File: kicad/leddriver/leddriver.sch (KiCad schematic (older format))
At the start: 19 parts, among them J1 Conn_01x01_Male, J2 Conn_01x02_Male, Q1 2N3904, SW1 SW_Push, U1 TLC555xP, U2 TLC555xP

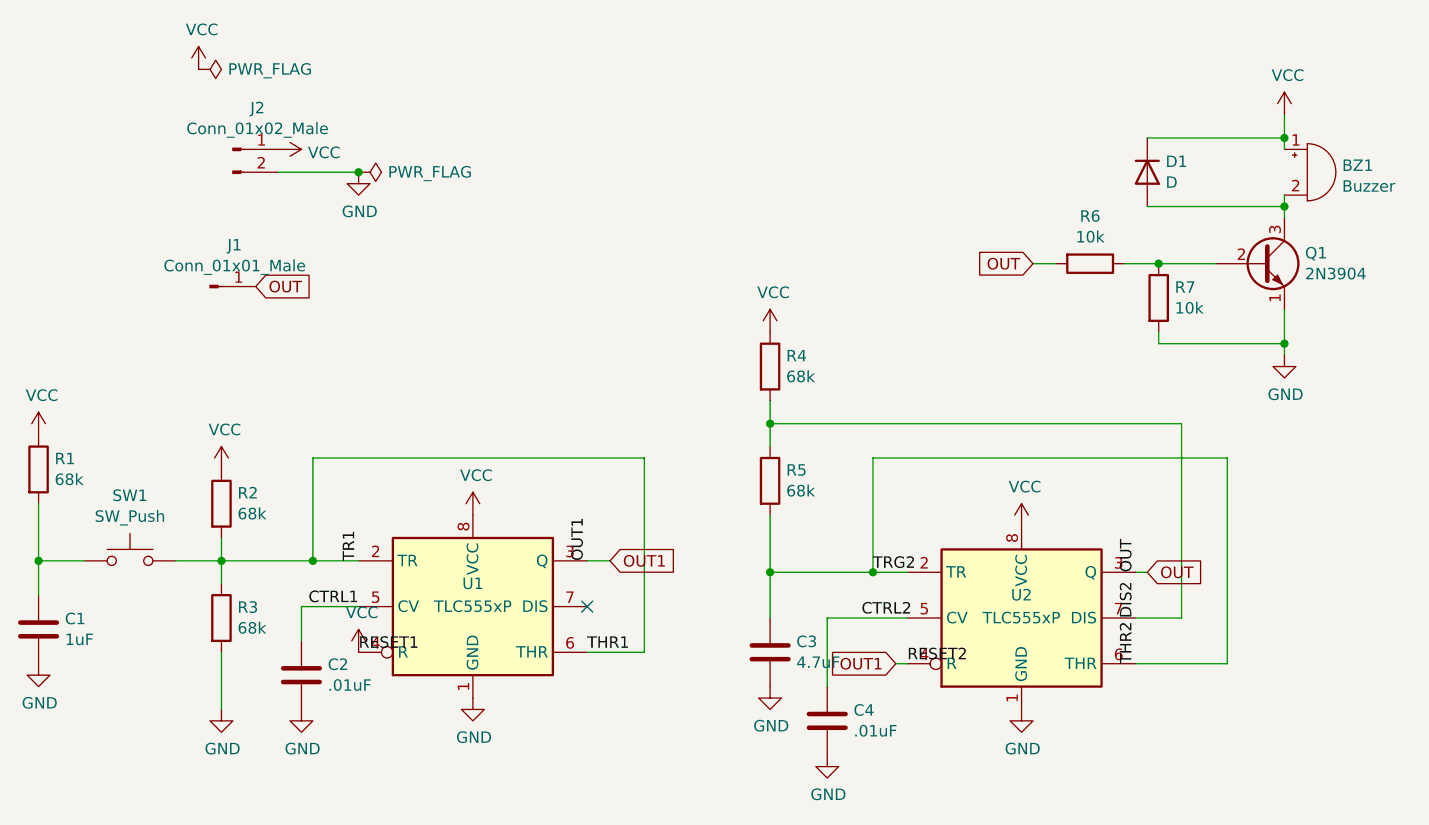
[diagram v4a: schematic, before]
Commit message: update according to new findings on breadboard.
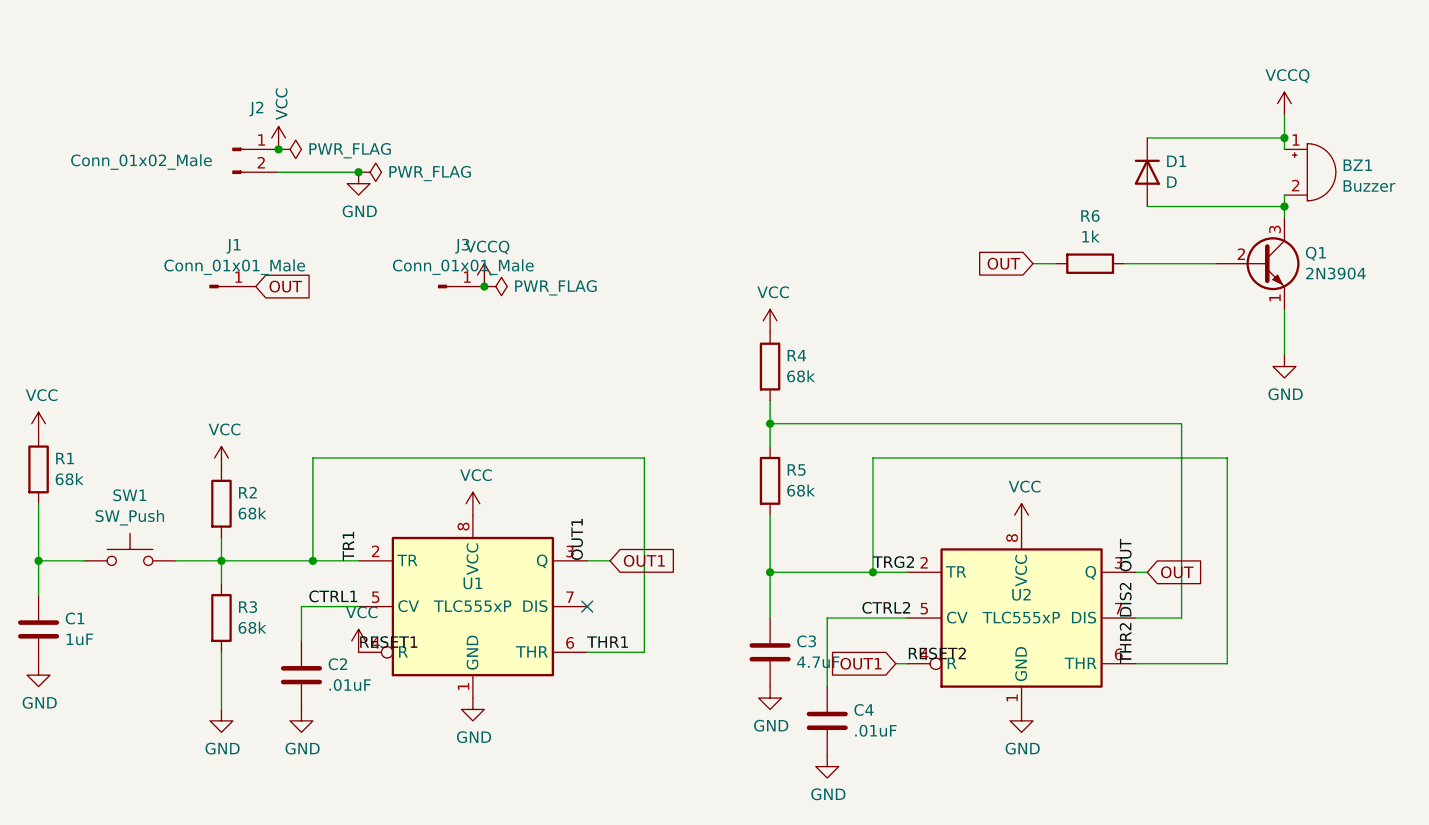
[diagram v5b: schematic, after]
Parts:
- removed R7: 10k, Resistor_THT:R_Axial_DIN0204_L3.6mm_D1.6mm_P2.54mm_Vertical, symbol Device:R
- added J3: Conn_01x01_Male, Connector_PinHeader_2.54mm:PinHeader_1x01_P2.54mm_Vertical, symbol Connector:Conn_01x01_Male
- R6: value 10k -> 1k
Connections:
- net VCC: no longer BZ1.1 (-), D1.1 (K)
- new net VCCQ: BZ1.1 (-), D1.1 (K), J3.1 (Pin_1)
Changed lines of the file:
@@
 L power:PWR_FLAG #FLG0101
 U 1 1 5F9073BF
-P 4350 750
-F 0 "#FLG0101" H 4350 825 50  0001 C CNN
-F 1 "PWR_FLAG" V 4350 878 50  0000 L CNN
-F 2 "" H 4350 750 50  0001 C CNN
-F 3 "~" H 4350 750 50  0001 C CNN
-	1    4350 750
+P 4700 1100
+F 0 "#FLG0101" H 4700 1175 50  0001 C CNN
+F 1 "PWR_FLAG" V 4700 1228 50  0000 L CNN
+F 2 "" H 4700 1100 50  0001 C CNN
+F 3 "~" H 4700 1100 50  0001 C CNN
+	1    4700 1100
 	0    1    1    0
 $EndComp
@@
 Text GLabel 8500 2950 2    50   Input ~ 0
 OUT
-$Comp
-L Connector:Conn_01x02_Male J2
-U 1 1 5F9522AD
-P 4500 1100
-F 0 "J2" H 4608 1281 50  0000 C CNN
-F 1 "Conn_01x02_Male" H 4608 1190 50  0000 C CNN
-F 2 "Connector_PinSocket_2.54mm:PinSocket_1x02_P2.54mm_Vertical" H 4500 1100 50  0001 C CNN
-F 3 "~" H 4500 1100 50  0001 C CNN
-	1    4500 1100
-	1    0    0    -1
-$EndComp
 Connection ~ 5050 1200
-$Comp
-L Connector:Conn_01x01_Male J1
-U 1 1 5F9568D2
-P 4400 1700
-F 0 "J1" H 4508 1881 50  0000 C CNN
-F 1 "Conn_01x01_Male" H 4508 1790 50  0000 C CNN
-F 2 "Connector_PinHeader_2.54mm:PinHeader_1x01_P2.54mm_Vertical" H 4400 1700 50  0001 C CNN
-F 3 "~" H 4400 1700 50  0001 C CNN
-	1    4400 1700
-	1    0    0    -1
-$EndComp
-$Comp
-L power:VCC #PWR0104
-U 1 1 5F974E8A
-P 4350 750
-F 0 "#PWR0104" H 4350 600 50  0001 C CNN
-F 1 "VCC" H 4365 923 50  0000 C CNN
-F 2 "" H 4350 750 50  0001 C CNN
-F 3 "" H 4350 750 50  0001 C CNN
-	1    4350 750
-	1    0    0    -1
-$EndComp
 $Comp
 L power:VCC #PWR0105
@@
 F 3 "" H 4700 1100 50  0001 C CNN
 	1    4700 1100
-	0    1    1    0
+	1    0    0    -1
 $EndComp
 $Comp
@@
 F 3 "" H 9100 2000 50  0001 C CNN
 	1    9100 2000
-	1    0    0    -1
-$EndComp
-$Comp
-L power:VCC #PWR0114
-U 1 1 5F9A00D1
-P 9100 950
-F 0 "#PWR0114" H 9100 800 50  0001 C CNN
-F 1 "VCC" H 9115 1123 50  0000 C CNN
-F 2 "" H 9100 950 50  0001 C CNN
-F 3 "" H 9100 950 50  0001 C CNN
-	1    9100 950
 	1    0    0    -1
 $EndComp
@@
 	9100 1050 9100 1100
 Wire Wire Line
-	9100 1800 9100 1950
-Wire Wire Line
 	4450 2900 4850 2900
 $Comp
@@
 	3650 2900 3650 3050
 $Comp
-L Device:R R7
-U 1 1 5F947F9D
-P 8550 1750
-F 0 "R7" H 8620 1796 50  0000 L CNN
-F 1 "10k" H 8620 1705 50  0000 L CNN
-F 2 "Resistor_THT:R_Axial_DIN0204_L3.6mm_D1.6mm_P2.54mm_Vertical" V 8480 1750 50  0001 C CNN
-F 3 "~" H 8550 1750 50  0001 C CNN
-	1    8550 1750
-	1    0    0    -1
-$EndComp
-$Comp
 L Device:R R6
 U 1 1 5F949B69
 P 8250 1600
 F 0 "R6" V 8043 1600 50  0000 C CNN
-F 1 "10k" V 8134 1600 50  0000 C CNN
+F 1 "1k" V 8134 1600 50  0000 C CNN
 F 2 "Resistor_THT:R_Axial_DIN0204_L3.6mm_D1.6mm_P2.54mm_Vertical" V 8180 1600 50  0001 C CNN
 F 3 "~" H 8250 1600 50  0001 C CNN
@@
 	8000 1600 8100 1600
 Wire Wire Line
-	8400 1600 8550 1600
-Wire Wire Line
-	8550 1600 8800 1600
-Connection ~ 8550 1600
-Wire Wire Line
-	8550 1900 8550 1950
-Wire Wire Line
-	8550 1950 9100 1950
-Connection ~ 9100 1950
-Wire Wire Line
-	9100 1950 9100 2000
-Wire Wire Line
 	4250 2900 4450 2900
 Wire Wire Line
 	3650 2900 3850 2900
+Wire Wire Line
+	8400 1600 8800 1600
+Wire Wire Line
+	9100 1800 9100 2000
+$Comp
+L power:VCCQ #PWR01
+U 1 1 5F9590BA
+P 9100 950
+F 0 "#PWR01" H 9100 800 50  0001 C CNN
+F 1 "VCCQ" H 9115 1123 50  0000 C CNN
+F 2 "" H 9100 950 50  0001 C CNN
+F 3 "" H 9100 950 50  0001 C CNN
+	1    9100 950
+	1    0    0    -1
+$EndComp
+$Comp
+L power:VCCQ #PWR07
+U 1 1 5F95B00B
+P 5600 1700
+F 0 "#PWR07" H 5600 1550 50  0001 C CNN
+F 1 "VCCQ" H 5615 1873 50  0000 C CNN
+F 2 "" H 5600 1700 50  0001 C CNN
+F 3 "" H 5600 1700 50  0001 C CNN
+	1    5600 1700
+	1    0    0    -1
+$EndComp
+$Comp
+L power:PWR_FLAG #FLG01
+U 1 1 5F95C0C3
+P 5600 1700
+F 0 "#FLG01" H 5600 1775 50  0001 C CNN
+F 1 "PWR_FLAG" V 5600 1828 50  0000 L CNN
+F 2 "" H 5600 1700 50  0001 C CNN
+F 3 "~" H 5600 1700 50  0001 C CNN
+	1    5600 1700
+	0    1    1    0
+$EndComp
+Connection ~ 5600 1700
+$Comp
+L Connector:Conn_01x01_Male J1
+U 1 1 5F9568D2
+P 4400 1700
+F 0 "J1" H 4508 1881 50  0000 C CNN
+F 1 "Conn_01x01_Male" H 4508 1790 50  0000 C CNN
+F 2 "Connector_PinHeader_2.54mm:PinHeader_1x01_P2.54mm_Vertical" H 4400 1700 50  0001 C CNN
+F 3 "~" H 4400 1700 50  0001 C CNN
+	1    4400 1700
+	1    0    0    -1
+$EndComp
+$Comp
+L Connector:Conn_01x02_Male J2
+U 1 1 5F9522AD
+P 4500 1100
+F 0 "J2" H 4608 1281 50  0000 C CNN
+F 1 "Conn_01x02_Male" H 4100 1050 50  0000 C CNN
+F 2 "Connector_PinSocket_2.54mm:PinSocket_1x02_P2.54mm_Vertical" H 4500 1100 50  0001 C CNN
+F 3 "~" H 4500 1100 50  0001 C CNN
+	1    4500 1100
+	1    0    0    -1
+$EndComp
+$Comp
+L Connector:Conn_01x01_Male J3
+U 1 1 5F95A9DE
+P 5400 1700
+F 0 "J3" H 5508 1881 50  0000 C CNN
+F 1 "Conn_01x01_Male" H 5508 1790 50  0000 C CNN
+F 2 "Connector_PinHeader_2.54mm:PinHeader_1x01_P2.54mm_Vertical" H 5400 1700 50  0001 C CNN
+F 3 "~" H 5400 1700 50  0001 C CNN
+	1    5400 1700
+	1    0    0    -1
+$EndComp
+Connection ~ 4700 1100
 $EndSCHEMATC

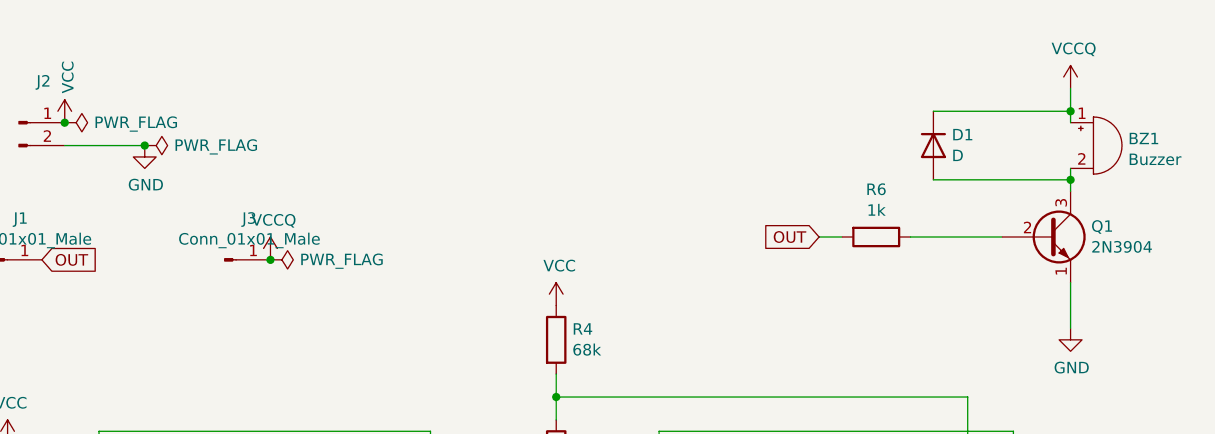
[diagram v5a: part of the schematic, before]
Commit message: chnage the schematic
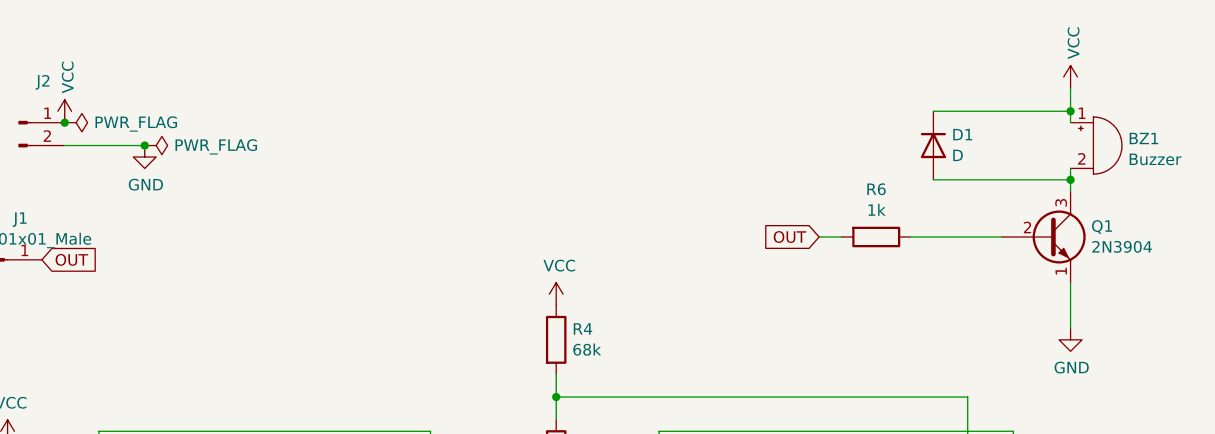
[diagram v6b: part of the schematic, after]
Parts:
- removed J3: Conn_01x01_Male, Connector_PinHeader_2.54mm:PinHeader_1x01_P2.54mm_Vertical, symbol Connector:Conn_01x01_Male
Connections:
- net VCCQ is gone; now on net VCC: BZ1.1 (-), D1.1 (K)
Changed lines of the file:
@@
 	9100 1800 9100 2000
-$Comp
-L power:VCCQ #PWR01
-U 1 1 5F9590BA
-P 9100 950
-F 0 "#PWR01" H 9100 800 50  0001 C CNN
-F 1 "VCCQ" H 9115 1123 50  0000 C CNN
-F 2 "" H 9100 950 50  0001 C CNN
-F 3 "" H 9100 950 50  0001 C CNN
-	1    9100 950
-	1    0    0    -1
-$EndComp
-$Comp
-L power:VCCQ #PWR07
-U 1 1 5F95B00B
-P 5600 1700
-F 0 "#PWR07" H 5600 1550 50  0001 C CNN
-F 1 "VCCQ" H 5615 1873 50  0000 C CNN
-F 2 "" H 5600 1700 50  0001 C CNN
-F 3 "" H 5600 1700 50  0001 C CNN
-	1    5600 1700
-	1    0    0    -1
-$EndComp
-$Comp
-L power:PWR_FLAG #FLG01
-U 1 1 5F95C0C3
-P 5600 1700
-F 0 "#FLG01" H 5600 1775 50  0001 C CNN
-F 1 "PWR_FLAG" V 5600 1828 50  0000 L CNN
-F 2 "" H 5600 1700 50  0001 C CNN
-F 3 "~" H 5600 1700 50  0001 C CNN
-	1    5600 1700
-	0    1    1    0
-$EndComp
-Connection ~ 5600 1700
 $Comp
 L Connector:Conn_01x01_Male J1
@@
 	1    0    0    -1
 $EndComp
+Connection ~ 4700 1100
 $Comp
-L Connector:Conn_01x01_Male J3
-U 1 1 5F95A9DE
-P 5400 1700
-F 0 "J3" H 5508 1881 50  0000 C CNN
-F 1 "Conn_01x01_Male" H 5508 1790 50  0000 C CNN
-F 2 "Connector_PinHeader_2.54mm:PinHeader_1x01_P2.54mm_Vertical" H 5400 1700 50  0001 C CNN
-F 3 "~" H 5400 1700 50  0001 C CNN
-	1    5400 1700
+L power:VCC #PWR01
+U 1 1 5F95AEEF
+P 9100 950
+F 0 "#PWR01" H 9100 800 50  0001 C CNN
+F 1 "VCC" V 9115 1078 50  0000 L CNN
+F 2 "" H 9100 950 50  0001 C CNN
+F 3 "" H 9100 950 50  0001 C CNN
+	1    9100 950
 	1    0    0    -1
 $EndComp
-Connection ~ 4700 1100
 $EndSCHEMATC

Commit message: Add bigger pads and track
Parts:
- C1, C2, C3, C4: footprint Capacitor_THT:C_Radial_D4.0mm_H5.0mm_P1.50mm -> Capacitor_THT:C_Radial_D8.0mm_H7.0mm_P3.50mm
- R1, R2, R3, R4, R5, R6: footprint Resistor_THT:R_Axial_DIN0204_L3.6mm_D1.6mm_P2.54mm_Vertical -> Resistor_THT:R_Axial_DIN0204_L3.6mm_D1.6mm_P5.08mm_Horizontal
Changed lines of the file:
@@
 F 0 "R1" H 3720 2546 50  0000 L CNN
 F 1 "68k" H 3720 2455 50  0000 L CNN
-F 2 "Resistor_THT:R_Axial_DIN0204_L3.6mm_D1.6mm_P2.54mm_Vertical" V 3580 2500 50  0001 C CNN
+F 2 "Resistor_THT:R_Axial_DIN0204_L3.6mm_D1.6mm_P5.08mm_Horizontal" V 3580 2500 50  0001 C CNN
 F 3 "~" H 3650 2500 50  0001 C CNN
 	1    3650 2500
@@
 F 0 "C1" H 3765 3246 50  0000 L CNN
 F 1 "1uF" H 3765 3155 50  0000 L CNN
-F 2 "Capacitor_THT:C_Radial_D4.0mm_H5.0mm_P1.50mm" H 3688 3050 50  0001 C CNN
+F 2 "Capacitor_THT:C_Radial_D8.0mm_H7.0mm_P3.50mm" H 3688 3050 50  0001 C CNN
 F 3 "~" H 3650 3200 50  0001 C CNN
 	1    3650 3200
@@
 F 0 "R2" H 4520 2696 50  0000 L CNN
 F 1 "68k" H 4520 2605 50  0000 L CNN
-F 2 "Resistor_THT:R_Axial_DIN0204_L3.6mm_D1.6mm_P2.54mm_Vertical" V 4380 2650 50  0001 C CNN
+F 2 "Resistor_THT:R_Axial_DIN0204_L3.6mm_D1.6mm_P5.08mm_Horizontal" V 4380 2650 50  0001 C CNN
 F 3 "~" H 4450 2650 50  0001 C CNN
 	1    4450 2650
@@
 F 0 "R3" H 4520 3196 50  0000 L CNN
 F 1 "68k" H 4520 3105 50  0000 L CNN
-F 2 "Resistor_THT:R_Axial_DIN0204_L3.6mm_D1.6mm_P2.54mm_Vertical" V 4380 3150 50  0001 C CNN
+F 2 "Resistor_THT:R_Axial_DIN0204_L3.6mm_D1.6mm_P5.08mm_Horizontal" V 4380 3150 50  0001 C CNN
 F 3 "~" H 4450 3150 50  0001 C CNN
 	1    4450 3150
@@
 F 0 "C2" H 4915 3446 50  0000 L CNN
 F 1 ".01uF" H 4915 3355 50  0000 L CNN
-F 2 "Capacitor_THT:C_Radial_D4.0mm_H5.0mm_P1.50mm" H 4838 3250 50  0001 C CNN
+F 2 "Capacitor_THT:C_Radial_D8.0mm_H7.0mm_P3.50mm" H 4838 3250 50  0001 C CNN
 F 3 "~" H 4800 3400 50  0001 C CNN
 	1    4800 3400
@@
 F 0 "R5" H 6920 2596 50  0000 L CNN
 F 1 "68k" H 6920 2505 50  0000 L CNN
-F 2 "Resistor_THT:R_Axial_DIN0204_L3.6mm_D1.6mm_P2.54mm_Vertical" V 6780 2550 50  0001 C CNN
+F 2 "Resistor_THT:R_Axial_DIN0204_L3.6mm_D1.6mm_P5.08mm_Horizontal" V 6780 2550 50  0001 C CNN
 F 3 "~" H 6850 2550 50  0001 C CNN
 	1    6850 2550
@@
 F 0 "R4" H 6920 2096 50  0000 L CNN
 F 1 "68k" H 6920 2005 50  0000 L CNN
-F 2 "Resistor_THT:R_Axial_DIN0204_L3.6mm_D1.6mm_P2.54mm_Vertical" V 6780 2050 50  0001 C CNN
+F 2 "Resistor_THT:R_Axial_DIN0204_L3.6mm_D1.6mm_P5.08mm_Horizontal" V 6780 2050 50  0001 C CNN
 F 3 "~" H 6850 2050 50  0001 C CNN
 	1    6850 2050
@@
 F 0 "C3" H 6965 3346 50  0000 L CNN
 F 1 "4.7uF" H 6965 3255 50  0000 L CNN
-F 2 "Capacitor_THT:C_Radial_D4.0mm_H5.0mm_P1.50mm" H 6888 3150 50  0001 C CNN
+F 2 "Capacitor_THT:C_Radial_D8.0mm_H7.0mm_P3.50mm" H 6888 3150 50  0001 C CNN
 F 3 "~" H 6850 3300 50  0001 C CNN
 	1    6850 3300
@@
 F 0 "C4" H 7215 3646 50  0000 L CNN
 F 1 ".01uF" H 7215 3555 50  0000 L CNN
-F 2 "Capacitor_THT:C_Radial_D4.0mm_H5.0mm_P1.50mm" H 7138 3450 50  0001 C CNN
+F 2 "Capacitor_THT:C_Radial_D8.0mm_H7.0mm_P3.50mm" H 7138 3450 50  0001 C CNN
 F 3 "~" H 7100 3600 50  0001 C CNN
 	1    7100 3600
@@
 F 0 "R6" V 8043 1600 50  0000 C CNN
 F 1 "1k" V 8134 1600 50  0000 C CNN
-F 2 "Resistor_THT:R_Axial_DIN0204_L3.6mm_D1.6mm_P2.54mm_Vertical" V 8180 1600 50  0001 C CNN
+F 2 "Resistor_THT:R_Axial_DIN0204_L3.6mm_D1.6mm_P5.08mm_Horizontal" V 8180 1600 50  0001 C CNN
 F 3 "~" H 8250 1600 50  0001 C CNN
 	1    8250 1600
